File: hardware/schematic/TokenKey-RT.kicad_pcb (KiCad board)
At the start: 4 copper layers, 50 x 40 mm, 103 parts, among them J1 USB-C, J2 Header 1x04 P2.54 H3.0 (OLED), J3 TC2030-NL, Q1 AO3401A, SW1 SW_BOOT, SW2 EC11E18244A5, SW3 BTN1, SW4 BTN2, U1 MIMXRT1062DVL6B, U2 AP2112K-3.3TRG1, U3 TLV62569DBVR, U4 W25Q64JVSSIQ, U5 APS6404L-3SQR-ZR, U6 USBLC6-2SC6, Y1 24MHz 12pF, Y2 32.768kHz 12.5pF

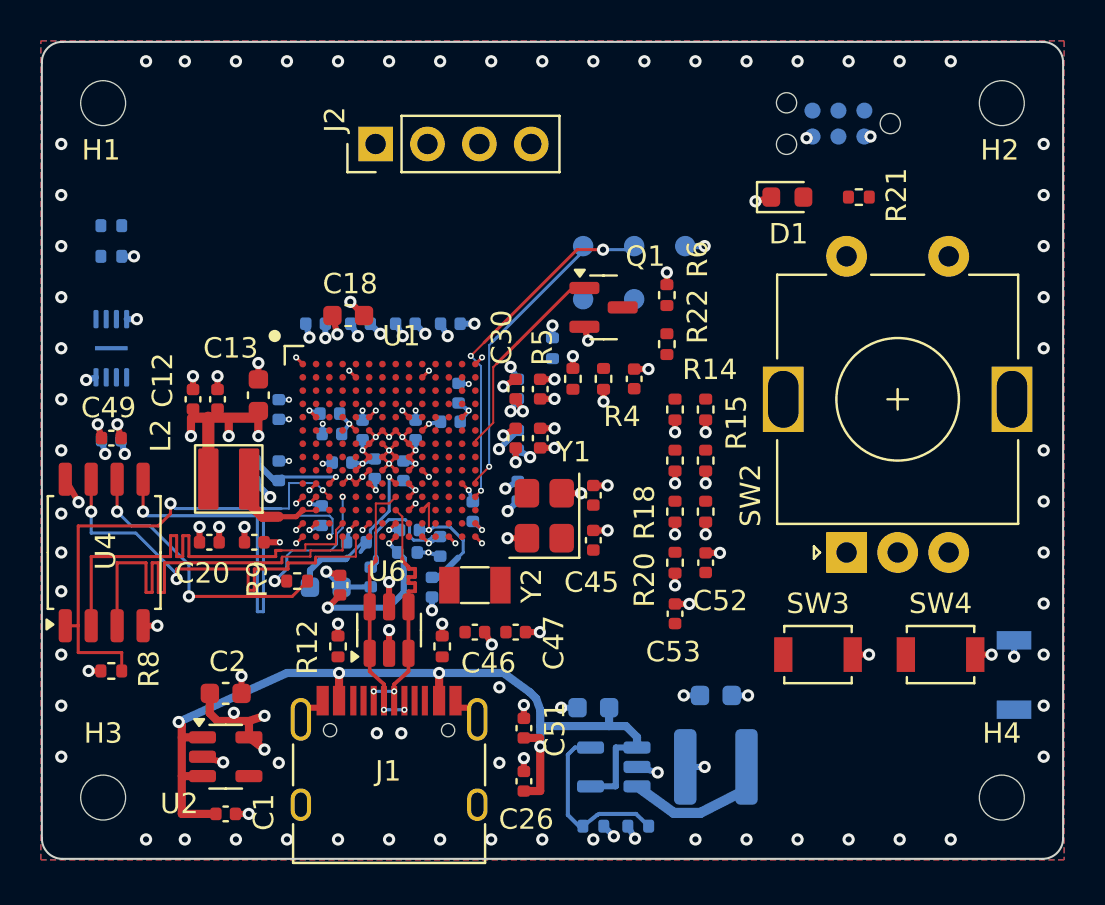
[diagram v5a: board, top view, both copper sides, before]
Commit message: Route BOOT_MODE0/BOOT_MODE0_Q and BOOT_MODE1 to SW_BOOT (Group A1b)
Part of #60
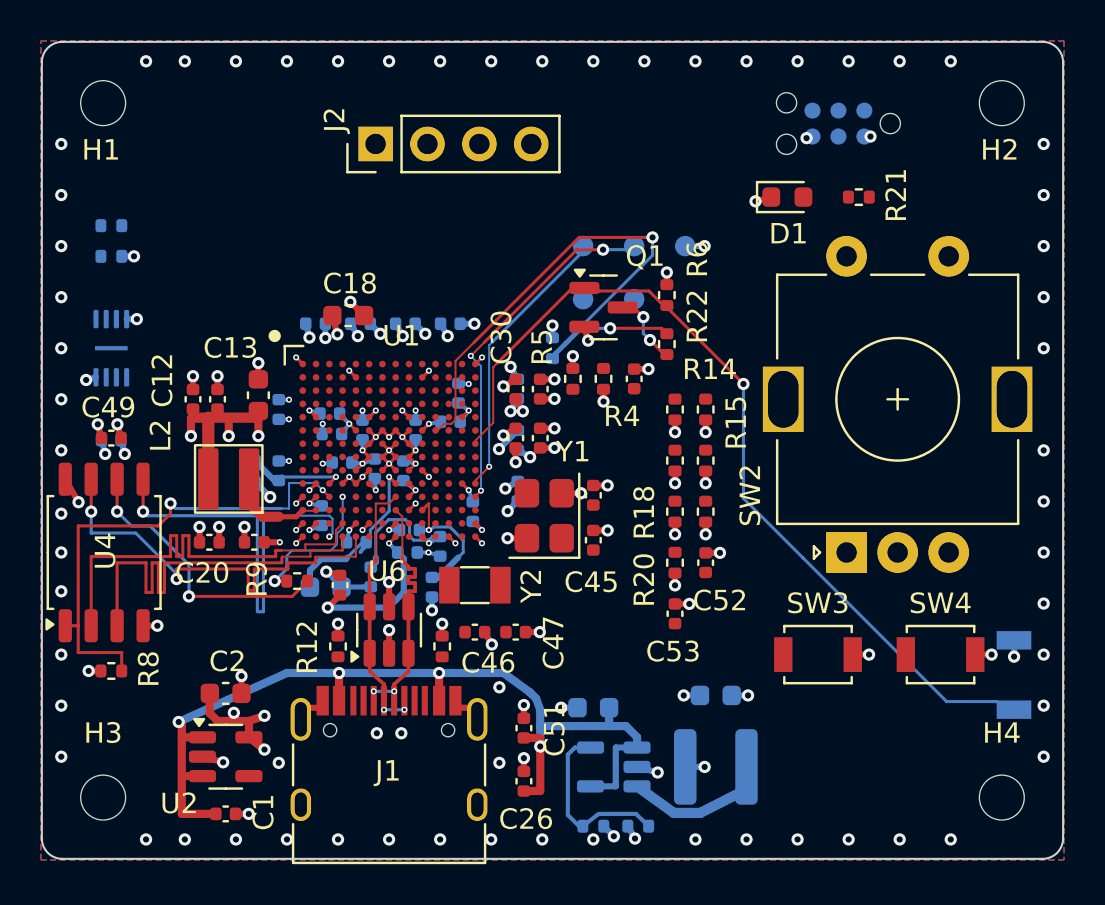
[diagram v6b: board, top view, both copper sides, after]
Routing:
- net BOOT_MODE1: track 10.1 -> 42.9 mm, vias 0 -> 1
- net BOOT_MODE0: track 0.00 -> 30.5 mm, vias 0 -> 2
- net BOOT_MODE0_Q: track 0.00 -> 3.51 mm, vias 0 -> 2

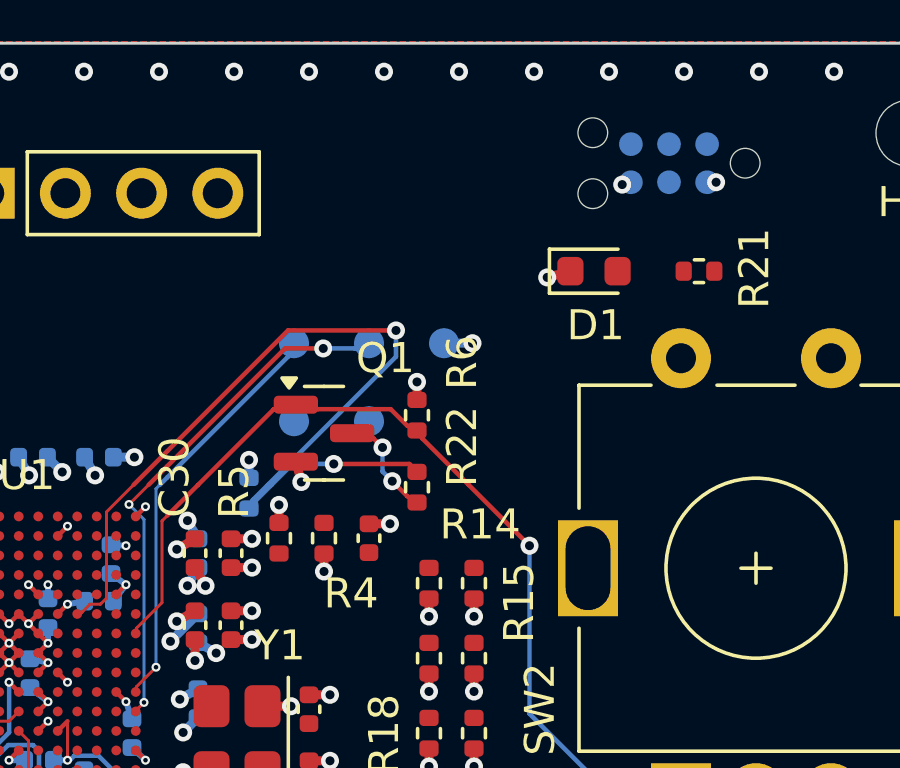
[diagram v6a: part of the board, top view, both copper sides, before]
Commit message: Route POR_B R4/C48/TP4/J3 side (M7 ball pending)
Part of #60
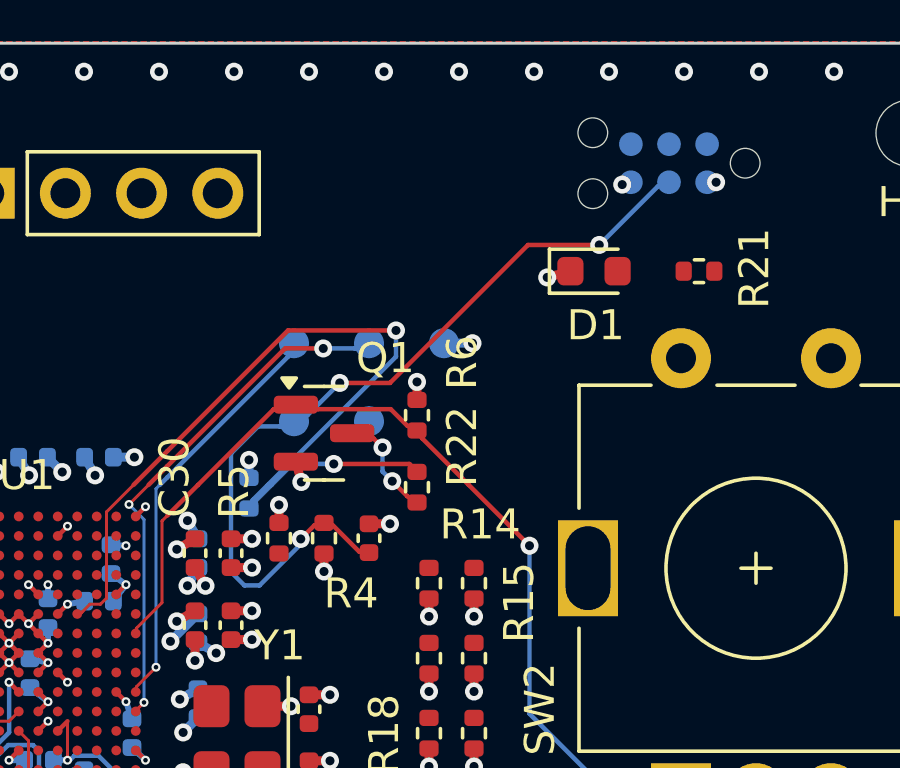
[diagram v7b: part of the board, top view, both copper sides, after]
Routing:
- net POR_B: track 0.00 -> 28.3 mm, vias 0 -> 3
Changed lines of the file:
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@@
+	)
+	(segment
+		(start 27.5 15.99)
+		(end 27.175 16.075)
+		(width 0.15)
+		(layer "F.Cu")
+		(net 14)
+	)
+	(segment
+		(start 29.7 11.325)
+		(end 34.3 6.725)
+		(width 0.15)
+		(layer "F.Cu")
+		(net 14)
+	)
+	(segment
+		(start 27.5 15.99)
+		(end 27.8 16.075)
+		(width 0.15)
+		(layer "F.Cu")
+		(net 14)
+	)
+	(segment
+		(start 27.8 16.075)
+		(end 28.675 16.95)
+		(width 0.15)
+		(layer "F.Cu")
+		(net 14)
+	)
+	(segment
+		(start 28.675 16.95)
+		(end 29 16.98)
+		(width 0.15)
+		(layer "F.Cu")
+		(net 14)
+	)
+	(segment
+		(start 34.3 6.725)
+		(end 36.675 6.725)
+		(width 0.15)
+		(layer "F.Cu")
+		(net 14)
+	)
+	(segment
+		(start 28.025 11.325)
+		(end 29.7 11.325)
+		(width 0.15)
+		(layer "F.Cu")
+		(net 14)
+	)
+	(segment
+		(start 27.175 16.075)
+		(end 26.725 16.524999)
+		(width 0.15)
+		(layer "F.Cu")
+		(net 14)
+	)
+	(via
+		(at 26.725 16.524999)
+		(size 0.6)
+		(drill 0.3)
+		(layers "F.Cu" "B.Cu")
+		(tenting front back)
+		(net 14)
+	)
+	(via
+		(at 36.675 6.725)
+		(size 0.6)
+		(drill 0.3)
+		(layers "F.Cu" "B.Cu")
+		(tenting front back)
+		(net 14)
+	)
+	(via
+		(at 28.025 11.325)
+		(size 0.6)
+		(drill 0.3)
+		(layers "F.Cu" "B.Cu")
+		(tenting front back)
+		(net 14)
+	)
+	(segment
+		(start 26.725 16.7)
+		(end 25.35 18.075)
+		(width 0.15)
+		(layer "B.Cu")
+		(net 14)
+	)
+	(segment
+		(start 25.3 12.775)
+		(end 26.025 12.775)
+		(width 0.15)
+		(layer "B.Cu")
+		(net 14)
+	)
+	(segment
+		(start 24.4 13.675)
+		(end 25.3 12.775)
+		(width 0.15)
+		(layer "B.Cu")
+		(net 14)
+	)
+	(segment
+		(start 26.5 12.6)
+		(end 26.95 12.4)
+		(width 0.15)
+		(layer "B.Cu")
+		(net 14)
+	)
+	(segment
+		(start 38.625 4.775)
+		(end 39 4.635)
+		(width 0.15)
+		(layer "B.Cu")
+		(net 14)
+	)
+	(segment
+		(start 26.95 12.4)
+		(end 28.025 11.325)
+		(width 0.15)
+		(layer "B.Cu")
+		(net 14)
+	)
+	(segment
+		(start 24.85 18.075)
+		(end 24.4 17.625)
+		(width 0.15)
+		(layer "B.Cu")
+		(net 14)
+	)
+	(segment
+		(start 25.35 18.075)
+		(end 24.85 18.075)
+		(width 0.15)
+		(layer "B.Cu")
+		(net 14)
+	)
+	(segment
+		(start 26.025 12.775)
+		(end 26.5 12.6)
+		(width 0.15)
+		(layer "B.Cu")
+		(net 14)
+	)
+	(segment
+		(start 36.675 6.725)
+		(end 38.625 4.775)
+		(width 0.15)
+		(layer "B.Cu")
+		(net 14)
+	)
+	(segment
+		(start 26.725 16.524999)
+		(end 26.725 16.7)
+		(width 0.15)
+		(layer "B.Cu")
+		(net 14)
+	)
+	(segment
+		(start 24.4 17.625)
+		(end 24.4 13.675)
+		(width 0.15)
+		(layer "B.Cu")
+		(net 14)
 	)
 	(segment

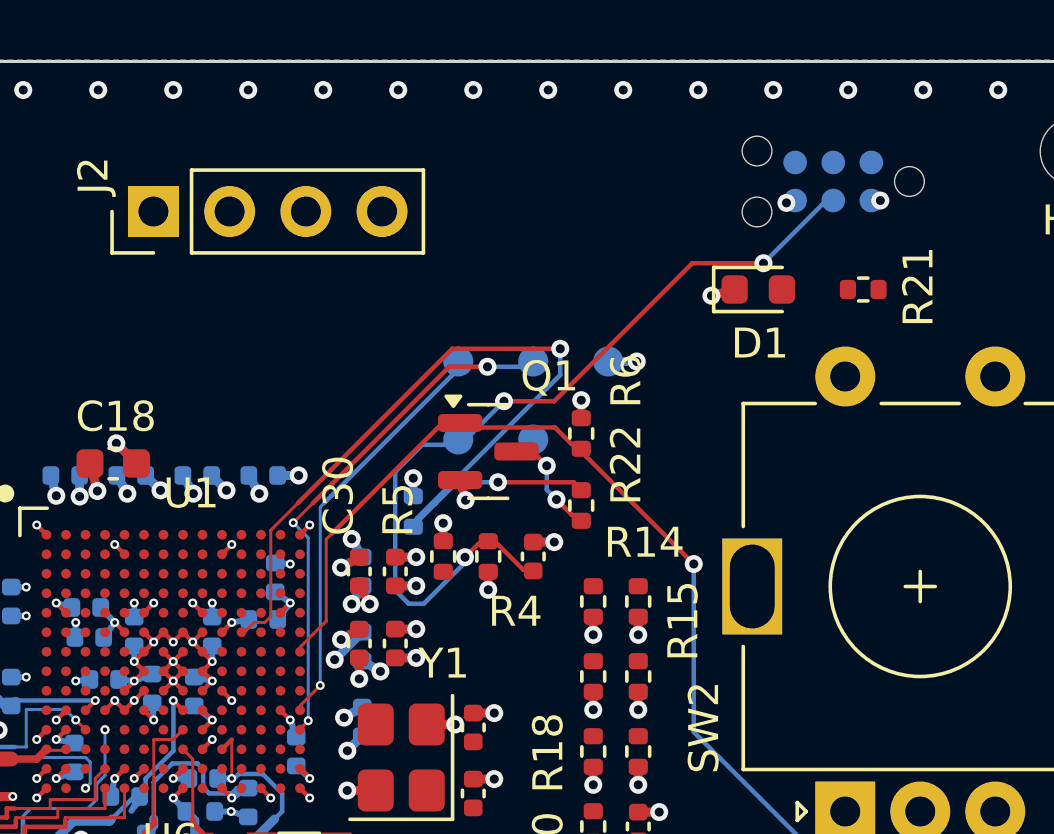
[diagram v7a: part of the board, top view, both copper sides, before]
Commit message: Route SWDIO/SWCLK/SWO to TC2030 J3 (Group A2)
Part of #60
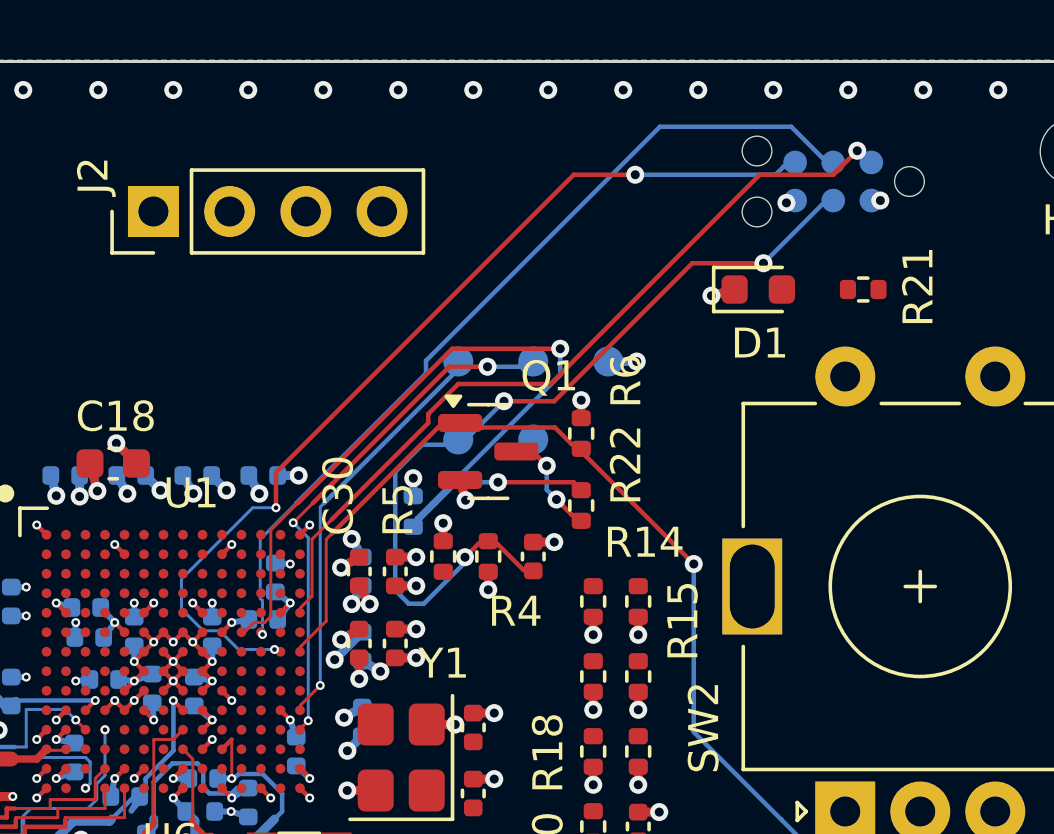
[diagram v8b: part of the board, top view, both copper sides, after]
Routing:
- net SWO: track 0.00 -> 31.7 mm, vias 0 -> 3
- net SWCLK: track 0.00 -> 28.8 mm, vias 0 -> 1
- net SWDIO: track 0.00 -> 26.9 mm, vias 0 -> 1
